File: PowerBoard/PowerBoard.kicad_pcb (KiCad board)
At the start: 2 copper layers, 127.5 x 70 mm, 107 parts, among them J1 V_IN, J10 GATE_PH_A, J11 GND, J12 V_IN, J13 TEMP_SENS, J2 PH_B, J3 PH_A, J4 PH_C, J5 CURR_SENS_PH_A, J6 CURR_SENS_PH_B, J7 CURR_SENS_PH_C, J8 GATE_PH_A, J9 GATE_PH_A, Q1 HSP0076A, Q10 HSP0076A, Q11 HSP0076A, Q12 HSP0076A, Q13 HSP0076A, Q14 HSP0076A, Q15 HSP0076A, Q16 HSP0076A, Q17 HSP0076A, Q18 HSP0076A, Q2 HSP0076A, Q3 HSP0076A, Q4 HSP0076A, Q5 HSP0076A, Q6 HSP0076A, Q7 HSP0076A, Q8 HSP0076A, Q9 HSP0076A

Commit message: updated board for new mosfets
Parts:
- removed C23, C24, C25: 2.2u, Capacitor_SMD:C_0603_1608Metric
- removed J10, J8, J9: GATE_PH_A, Connector_PinHeader_1.00mm:PinHeader_1x06_P1.00mm_Vertical
- removed J13: TEMP_SENS, Connector_PinHeader_1.00mm:PinHeader_1x08_P1.00mm_Vertical
- removed R28, R29, R30: 10k, Resistor_SMD:R_0603_1608Metric
- added H1: MountingHole, MountingHole:MountingHole_2.2mm_M2, F.Cu at (207.6, 106.2)
- added H2: MountingHole, MountingHole:MountingHole_2.2mm_M2, F.Cu at (207.6, 153.1)
- added H3: MountingHole, MountingHole:MountingHole_2.2mm_M2, F.Cu at (342.6, 106.2)
- added H4: MountingHole, MountingHole:MountingHole_2.2mm_M2, F.Cu at (342.6, 153.2)
- D1, D10, D11, D12, D13, D14, D15, D16, D17, D18, D2, D3, D4, D5, D6, D7, D8, D9, R1, R19, R2, R20, R21, R22, R23, R24, R25, R26, R27, R3, R4, R5, R6, R7, R8, R9: moved to F.Cu
- J12: footprint Connector_PinHeader_1.00mm:PinHeader_1x02_P1.00mm_Vertical -> Connector_PinHeader_2.54mm:PinHeader_1x02_P2.54mm_Vertical
- J2, J3, J4, R10, R11, R12, R13, R14, R15, R16, R17, R18: moved to B.Cu
- J5: value CURR_SENS_PH_A -> PH_B_CONNECTOR; footprint Connector_PinHeader_1.00mm:PinHeader_1x04_P1.00mm_Vertical -> Connector_PinHeader_2.54mm:PinHeader_2x04_P2.54mm_Vertical
- J6: value CURR_SENS_PH_B -> PH_A_CONNECTOR; footprint Connector_PinHeader_1.00mm:PinHeader_1x04_P1.00mm_Vertical -> Connector_PinHeader_2.54mm:PinHeader_2x04_P2.54mm_Vertical
- J7: value CURR_SENS_PH_C -> PH_C_CONNECTOR; footprint Connector_PinHeader_1.00mm:PinHeader_1x04_P1.00mm_Vertical -> Connector_PinHeader_2.54mm:PinHeader_2x04_P2.54mm_Vertical
- Q1, Q10, Q11, Q12, Q13, Q14, Q15, Q16, Q17, Q18, Q2, Q3, Q4, Q5, Q6, Q7, Q8, Q9: footprint Package_TO_SOT_THT:TO-220-3_Horizontal_TabUp_withoutHole -> Package_TO_SOT_SMD:Infineon_PG-HSOF-8-1
- moved C20 299.7 mm to (41.6, 61.4), turned to 0 degrees
- moved C21 299.5 mm to (41.6, 79.0), turned to 0 degrees
- moved C19 293.5 mm to (41.6, 43.9), turned to 0 degrees
- moved C22 282.8 mm to (41.6, 96.5), turned to 0 degrees
- moved NTC3 121.7 mm to (299.2, 119.2), turned to 90 degrees
- moved NTC1 102.6 mm to (210.1, 119.5), turned to 90 degrees
- moved C9 95.3 mm to (336.0, 115.6)
- moved D13 93.7 mm to (328.4, 133.4)
- moved C8 93.1 mm to (336.0, 112.3)
- moved C7 91.0 mm to (336.0, 109.0)
- moved C6 88.0 mm to (291.2, 115.6)
- moved C18 86.7 mm to (336.0, 125.5)
- moved D10 85.9 mm to (284.1, 133.5)
- moved C5 85.6 mm to (291.2, 112.3)
- moved C17 84.7 mm to (336.0, 122.2)
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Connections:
- D10 pad 1: /GL_A -> /GL_B
- D11 pad 1: /GL_A -> /GL_B
- D12 pad 1: /GL_A -> /GL_B
- D13 pad 1: /GL_B -> /GL_C
- D14 pad 1: /GL_B -> /GL_C
- D15 pad 1: /GL_B -> /GL_C
- D16 pad 1: /GL_C -> /GH_C
- D17 pad 1: /GL_C -> /GH_C
- D18 pad 1: /GL_C -> /GH_C
- D4 pad 1: /GH_B -> /GL_A
- D5 pad 1: /GH_B -> /GL_A
- D6 pad 1: /GH_B -> /GL_A
- D7 pad 1: /GH_C -> /GH_B
- D8 pad 1: /GH_C -> /GH_B
- D9 pad 1: /GH_C -> /GH_B
- J5 pad 1: /SH_A -> /PH_B_IN+
- J5 pad 3: /PH_A -> GND
- J5 pad 4: GND -> /TEMP2
- J6 pad 1: /SH_B -> /PH_A_IN+
- J6 pad 3: /PH_B -> GND
- J6 pad 4: GND -> /TEMP
- J7 pad 1: /SH_C -> /PH_C_IN+
- J7 pad 3: /PH_C -> GND
- J7 pad 4: GND -> /TEMP3
- NTC2 pad 1: /VCC -> /VCC1
- NTC3 pad 1: /VCC -> /VCC2
- Q1 pad 2: V_IN -> /PH_A
- Q1 pad 3: /SH_A -> V_IN
- Q10 pad 1: Net-(D10-A) -> Net-(D4-A)
- Q10 pad 2: /SH_A -> /PH_A_IN+
- Q10 pad 3: GND -> /PH_A
- Q11 pad 1: Net-(D11-A) -> Net-(D5-A)
- Q11 pad 2: /SH_A -> /PH_A_IN+
- Q11 pad 3: GND -> /PH_A
- Q12 pad 1: Net-(D12-A) -> Net-(D6-A)
- Q12 pad 2: /SH_A -> /PH_A_IN+
- Q12 pad 3: GND -> /PH_A
- Q13 pad 1: Net-(D13-A) -> Net-(D10-A)
- Q13 pad 2: /SH_B -> /PH_B_IN+
- Q13 pad 3: GND -> /PH_B
- Q14 pad 1: Net-(D14-A) -> Net-(D11-A)
- Q14 pad 2: /SH_B -> /PH_B_IN+
- Q14 pad 3: GND -> /PH_B
- Q15 pad 1: Net-(D15-A) -> Net-(D12-A)
- Q15 pad 2: /SH_B -> /PH_B_IN+
- Q15 pad 3: GND -> /PH_B
- Q16 pad 1: Net-(D16-A) -> Net-(D13-A)
- Q16 pad 2: /SH_C -> /PH_C_IN+
- Q16 pad 3: GND -> /PH_C
- Q17 pad 1: Net-(D17-A) -> Net-(D14-A)
- Q17 pad 2: /SH_C -> /PH_C_IN+
- Q17 pad 3: GND -> /PH_C
- Q18 pad 1: Net-(D18-A) -> Net-(D15-A)
- Q18 pad 2: /SH_C -> /PH_C_IN+
- Q18 pad 3: GND -> /PH_C
- Q2 pad 2: V_IN -> /PH_A
- Q2 pad 3: /SH_A -> V_IN
- Q3 pad 2: V_IN -> /PH_A
- Q3 pad 3: /SH_A -> V_IN
- Q4 pad 1: Net-(D4-A) -> Net-(D7-A)
- Q4 pad 2: V_IN -> /PH_B
- Q4 pad 3: /SH_B -> V_IN
- Q5 pad 1: Net-(D5-A) -> Net-(D8-A)
- Q5 pad 2: V_IN -> /PH_B
- Q5 pad 3: /SH_B -> V_IN
- Q6 pad 1: Net-(D6-A) -> Net-(D9-A)
- Q6 pad 2: V_IN -> /PH_B
- Q6 pad 3: /SH_B -> V_IN
- Q7 pad 1: Net-(D7-A) -> Net-(D18-A)
- Q7 pad 2: V_IN -> /PH_C
- Q7 pad 3: /SH_C -> V_IN
- Q8 pad 1: Net-(D8-A) -> Net-(D17-A)
- Q8 pad 2: V_IN -> /PH_C
- Q8 pad 3: /SH_C -> V_IN
- Q9 pad 1: Net-(D9-A) -> Net-(D16-A)
- Q9 pad 2: V_IN -> /PH_C
- Q9 pad 3: /SH_C -> V_IN
- R10 pad 1: /PH_A -> GND
- R10 pad 2: /SH_A -> /PH_A_IN+
- R11 pad 1: /PH_B -> GND
- R11 pad 2: /SH_B -> /PH_B_IN+
- R12 pad 1: /PH_C -> GND
- R12 pad 2: /SH_C -> /PH_C_IN+
- R13 pad 1: /PH_A -> GND
- R13 pad 2: /SH_A -> /PH_A_IN+
- R14 pad 1: /PH_B -> GND
- R14 pad 2: /SH_B -> /PH_B_IN+
- R15 pad 1: /PH_C -> GND
- R15 pad 2: /SH_C -> /PH_C_IN+
- R16 pad 1: /PH_A -> GND
- R16 pad 2: /SH_A -> /PH_A_IN+
- R17 pad 1: /PH_B -> GND
- R17 pad 2: /SH_B -> /PH_B_IN+
- R18 pad 1: /PH_C -> GND
- R18 pad 2: /SH_C -> /PH_C_IN+
- R19 pad 2: Net-(D10-A) -> Net-(D4-A)
- R20 pad 2: Net-(D11-A) -> Net-(D5-A)
- R21 pad 2: Net-(D12-A) -> Net-(D6-A)
- R22 pad 2: Net-(D13-A) -> Net-(D10-A)
- R23 pad 2: Net-(D14-A) -> Net-(D11-A)
- R24 pad 2: Net-(D15-A) -> Net-(D12-A)
- R25 pad 2: Net-(D16-A) -> Net-(D13-A)
- R26 pad 2: Net-(D17-A) -> Net-(D14-A)
- R27 pad 2: Net-(D18-A) -> Net-(D15-A)
- R4 pad 2: Net-(D4-A) -> Net-(D7-A)
- R5 pad 2: Net-(D5-A) -> Net-(D8-A)
- R6 pad 2: Net-(D6-A) -> Net-(D9-A)
- R7 pad 2: Net-(D7-A) -> Net-(D18-A)
- R8 pad 2: Net-(D8-A) -> Net-(D17-A)
- R9 pad 2: Net-(D9-A) -> Net-(D16-A)
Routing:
- net GND: track 78.0 -> 303.0 mm, vias 524 -> 42
- net /VCC: track 90.4 -> 13.6 mm, vias 3 -> 0
- net /TEMP: track 79.7 -> 18.3 mm, vias 1 -> 0
- net V_IN: track 70.8 -> 10.5 mm
- net /PH_B_IN+: track 0.00 -> 46.0 mm
- net /PH_C_IN+: track 0.00 -> 44.6 mm
- net /PH_A_IN+: track 0.00 -> 43.8 mm
- net /SH_A: track 35.9 -> 0.00 mm, vias 10 -> 0
- net /GH_B: track 14.5 -> 46.0 mm
- net /GH_C: track 15.1 -> 46.0 mm
- net /GH_A: track 15.2 -> 46.0 mm
- net /SH_B: track 26.2 -> 0.00 mm, vias 10 -> 0
- net /SH_C: track 25.2 -> 0.00 mm, vias 10 -> 0
- net /TEMP2: track 44.7 -> 20.8 mm
- net /GL_C: track 18.7 -> 33.0 mm
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- added copper zone on B.Cu, net /PH_A
- added copper zone on B.Cu, net /PH_A_IN+
- added copper zone on B.Cu, net /PH_B
- added copper zone on B.Cu, net /PH_B_IN+
- added copper zone on B.Cu, net /PH_C
- added copper zone on B.Cu, net /PH_C_IN+
- removed copper zone on F.Cu, net /PH_A
- removed copper zone on F.Cu, net /PH_B
- removed copper zone on F.Cu, net /PH_C
- removed copper zone on F.Cu, net /SH_A
- removed copper zone on F.Cu, net /SH_B
- removed copper zone on F.Cu, net /SH_C
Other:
- board size 127.5 x 70 mm -> 145 x 57 mm
- board text added: "Designed by BREKESHEV BAKTIYAR myVESC POWER BOARD V0.1"

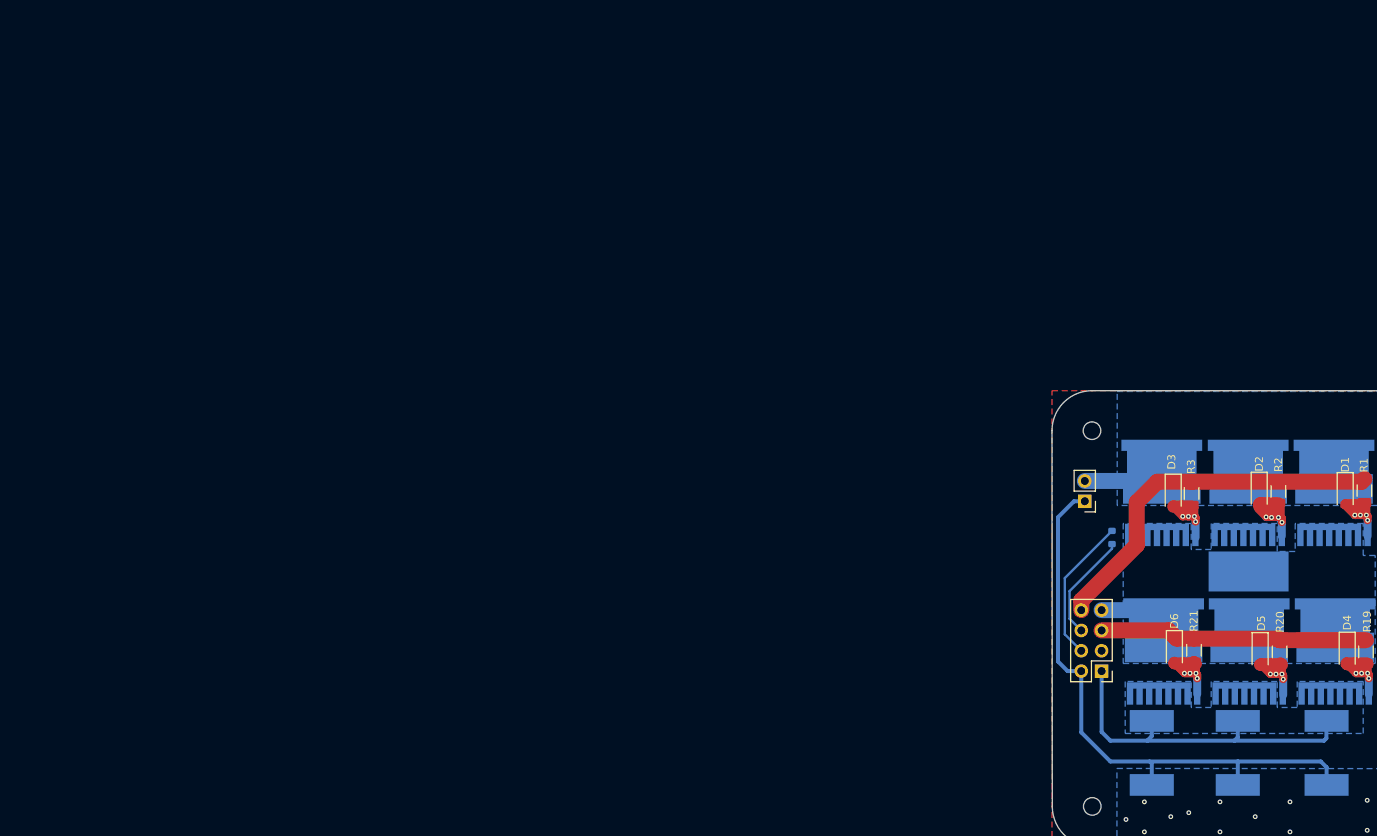
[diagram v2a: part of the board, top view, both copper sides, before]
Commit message: added resistor for shunts
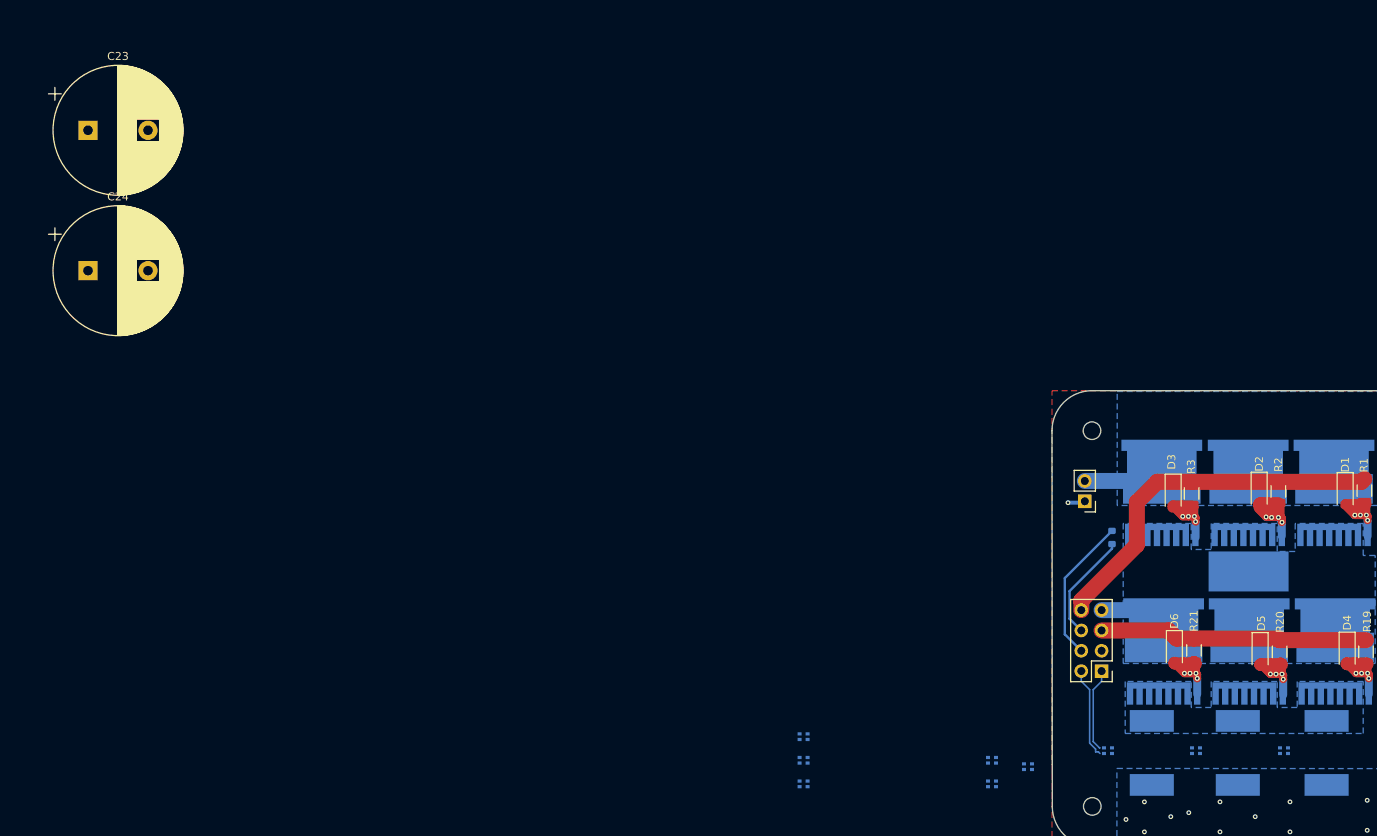
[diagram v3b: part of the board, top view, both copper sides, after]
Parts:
- added C23: 470u_200V, Capacitor_THT:CP_Radial_D16.0mm_P7.50mm, F.Cu at (82.1, 68.6)
- added C24: 470u_200V, Capacitor_THT:CP_Radial_D16.0mm_P7.50mm, F.Cu at (82.1, 86.2)
- added RN1: R_Pack02, Resistor_SMD:R_Array_Convex_2x0402, B.Cu at (231.6, 146.2)
- added RN2: R_Pack02, Resistor_SMD:R_Array_Convex_2x0402, B.Cu at (220.6, 146.2)
- added RN3: R_Pack02, Resistor_SMD:R_Array_Convex_2x0402, B.Cu at (209.6, 146.2)
- added RN4: R_Pack02, Resistor_SMD:R_Array_Convex_2x0402, B.Cu at (171.6, 144.4)
- added RN5: R_Pack02, Resistor_SMD:R_Array_Convex_2x0402, B.Cu at (171.6, 147.3)
- added RN6: R_Pack02, Resistor_SMD:R_Array_Convex_2x0402, B.Cu at (171.6, 150.3)
- added RN7: R_Pack02, Resistor_SMD:R_Array_Convex_2x0402, B.Cu at (199.6, 148.2)
- added RN8: R_Pack02, Resistor_SMD:R_Array_Convex_2x0402, B.Cu at (195.1, 147.3)
- added RN9: R_Pack02, Resistor_SMD:R_Array_Convex_2x0402, B.Cu at (195.1, 150.3)
- R10, R11, R12, R13, R14, R15, R16, R17, R18: value 0.0005R -> 0.0002R
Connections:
- J5 pad 1: /PH_B_IN+ -> /PH_B_IN_D+
- J5 pad 2: GND -> /PH_B_IN_D-
- J6 pad 1: /PH_A_IN+ -> /PH_A_IN_D+
- J6 pad 2: GND -> /PH_A_IN_D-
- J7 pad 1: /PH_C_IN+ -> /PH_C_IN_D+
- J7 pad 2: GND -> /PH_C_IN_D-
- Q10 pad 2: /PH_A_IN+ -> /A_D+
- Q11 pad 2: /PH_A_IN+ -> /A_D+
- Q12 pad 2: /PH_A_IN+ -> /A_D+
- Q13 pad 2: /PH_B_IN+ -> Net-(Q13-S)
- Q14 pad 2: /PH_B_IN+ -> Net-(Q13-S)
- Q15 pad 2: /PH_B_IN+ -> Net-(Q13-S)
- Q16 pad 2: /PH_C_IN+ -> Net-(Q16-S)
- Q17 pad 2: /PH_C_IN+ -> Net-(Q16-S)
- Q18 pad 2: /PH_C_IN+ -> Net-(Q16-S)
- R10 pad 2: /PH_A_IN+ -> /A_D+
- R11 pad 2: /PH_B_IN+ -> Net-(Q13-S)
- R12 pad 2: /PH_C_IN+ -> Net-(Q16-S)
- R13 pad 2: /PH_A_IN+ -> /A_D+
- R14 pad 2: /PH_B_IN+ -> Net-(Q13-S)
- R15 pad 2: /PH_C_IN+ -> Net-(Q16-S)
- R16 pad 2: /PH_A_IN+ -> /A_D+
- R17 pad 2: /PH_B_IN+ -> Net-(Q13-S)
- R18 pad 2: /PH_C_IN+ -> Net-(Q16-S)
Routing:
- net GND: track 303.0 -> 231.7 mm, vias 42 -> 43
- net /PH_B_IN+: track 46.0 -> 0.00 mm
- net (no net): track 0.00 -> 46.0 mm
- net Net-(Q16-S): track 0.00 -> 44.6 mm
- net /PH_C_IN+: track 44.6 -> 0.00 mm
- net /PH_A_IN+: track 43.8 -> 0.00 mm
- net /PH_A_IN_D-: track 0.00 -> 11.5 mm
- net /PH_A_IN_D+: track 0.00 -> 10.4 mm
- added copper zone on B.Cu, net /PH_A_IN_D+
- added copper zone on B.Cu, net /PH_B_IN_D+
- added copper zone on B.Cu, net /PH_C_IN_D+
- removed copper zone on B.Cu, net /PH_A_IN+
- removed copper zone on B.Cu, net /PH_B_IN+
- removed copper zone on B.Cu, net /PH_C_IN+

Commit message: new
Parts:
- removed RN1, RN2, RN3, RN4, RN5, RN6, RN7, RN8, RN9: R_Pack02, Resistor_SMD:R_Array_Convex_2x0402
- added R28: 10, Resistor_SMD:R_0201_0603Metric, B.Cu at (233.1, 145.2)
- added R29: 10, Resistor_SMD:R_0201_0603Metric, B.Cu at (233.1, 147.5)
- added R30: 10, Resistor_SMD:R_0201_0603Metric, B.Cu at (222.1, 145.2)
- added R31: 10, Resistor_SMD:R_0201_0603Metric, B.Cu at (222.1, 147.5)
- added R32: 10, Resistor_SMD:R_0201_0603Metric, B.Cu at (211.3, 145.2)
- added R33: 10, Resistor_SMD:R_0201_0603Metric, B.Cu at (211.3, 147.5)
- added R34: 10, Resistor_SMD:R_0201_0603Metric, B.Cu at (256.6, 145.2)
- added R35: 10, Resistor_SMD:R_0201_0603Metric, B.Cu at (256.6, 147.5)
- added R36: 10, Resistor_SMD:R_0201_0603Metric, B.Cu at (267.6, 145.2)
- added R37: 10, Resistor_SMD:R_0201_0603Metric, B.Cu at (267.6, 147.5)
- added R38: 10, Resistor_SMD:R_0201_0603Metric, B.Cu at (278.4, 145.2)
- added R39: 10, Resistor_SMD:R_0201_0603Metric, B.Cu at (278.4, 147.5)
- added R40: 10, Resistor_SMD:R_0201_0603Metric, B.Cu at (301.1, 145.2)
- added R41: 10, Resistor_SMD:R_0201_0603Metric, B.Cu at (301.1, 147.5)
- added R42: 10, Resistor_SMD:R_0201_0603Metric, B.Cu at (312.1, 145.2)
- added R43: 10, Resistor_SMD:R_0201_0603Metric, B.Cu at (312.1, 147.5)
- added R44: 10, Resistor_SMD:R_0201_0603Metric, B.Cu at (322.9, 145.2)
- added R45: 10, Resistor_SMD:R_0201_0603Metric, B.Cu at (322.9, 147.5)
- moved C23 41.5 mm to (85.0, 110.0), turned to 90 degrees
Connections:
- net /A_D+ renamed Net-(Q10-S)
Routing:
- net GND: track 231.7 -> 185.1 mm
- net (no net): track 46.0 -> 0.00 mm
- net /PH_C_IN_D-: track 0.00 -> 35.3 mm
- net /PH_B_IN_D-: track 0.00 -> 35.0 mm
- net /PH_C_IN_D+: track 0.00 -> 33.9 mm
- net /PH_B_IN_D+: track 0.00 -> 33.6 mm
- net Net-(Q16-S): track 44.6 -> 17.4 mm
- net /PH_A_IN_D-: track 11.5 -> 34.8 mm
- net /PH_A_IN_D+: track 10.4 -> 33.4 mm
- net Net-(Q10-S): track 0.04 -> 18.1 mm
- net Net-(Q13-S): track 0.00 -> 17.4 mm
- added copper zone on B.Cu, net Net-(Q10-S)
- added copper zone on B.Cu, net Net-(Q13-S)
- added copper zone on B.Cu, net Net-(Q16-S)
- removed copper zone on B.Cu, net /PH_A_IN_D+
- removed copper zone on B.Cu, net /PH_B_IN_D+
- removed copper zone on B.Cu, net /PH_C_IN_D+

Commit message: power board is done !
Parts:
- removed C22, C23, C24: 470u_200V, Capacitor_THT:CP_Radial_D16.0mm_P7.50mm
- moved C19 308.9 mm to (343.1, 111.0), turned to -90 degrees
- moved C20 308.4 mm to (343.2, 125.8), turned to -90 degrees
- moved C21 307.8 mm to (343.2, 140.3), turned to -90 degrees
- moved J1 0.16 mm to (332.9, 104.1)
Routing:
- net V_IN: track 10.5 -> 39.0 mm
- net Net-(D8-A): track 11.8 -> 14.0 mm
- net Net-(D17-A): track 11.8 -> 13.9 mm
- net Net-(D14-A): track 12.2 -> 14.4 mm
- net Net-(D9-A): track 11.8 -> 13.9 mm
- net Net-(D12-A): track 11.8 -> 13.9 mm
- net Net-(D3-A): track 11.9 -> 14.0 mm
- net Net-(D1-A): track 13.4 -> 15.6 mm
- net Net-(D18-A): track 11.8 -> 13.9 mm
- net Net-(D16-A): track 11.8 -> 13.9 mm
- net Net-(D13-A): track 12.5 -> 14.6 mm
- net Net-(D11-A): track 11.8 -> 13.9 mm
- net Net-(D7-A): track 11.8 -> 13.9 mm
- net Net-(D15-A): track 12.2 -> 14.4 mm
- net Net-(D10-A): track 11.8 -> 13.8 mm
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
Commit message: final
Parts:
- added C22: 470u_200V, Capacitor_THT:CP_Radial_D16.0mm_P7.50mm, F.Cu at (338.1, 142.1)
- added C23: 470u_200V, Capacitor_THT:CP_Radial_D16.0mm_P7.50mm, F.Cu at (345.3, 129.5)
- added C24: 470u_200V, Capacitor_THT:CP_Radial_D16.0mm_P7.50mm, F.Cu at (344.9, 114.6)
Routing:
- net V_IN: track 39.0 -> 54.6 mm
- net GND: vias 43 -> 238
